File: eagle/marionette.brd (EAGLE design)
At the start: 160.3 x 174 mm, 64 parts, among them J2 SWD_CONNECTOR, J3 2X10FE, J4 2X10FE, J5 2X10FE, J6 2X10FE, J7 2X10FE, U1 USB3318, U2 NCP705, U3 XCL206B, X1 ABS25-32.768KHZ-6-T

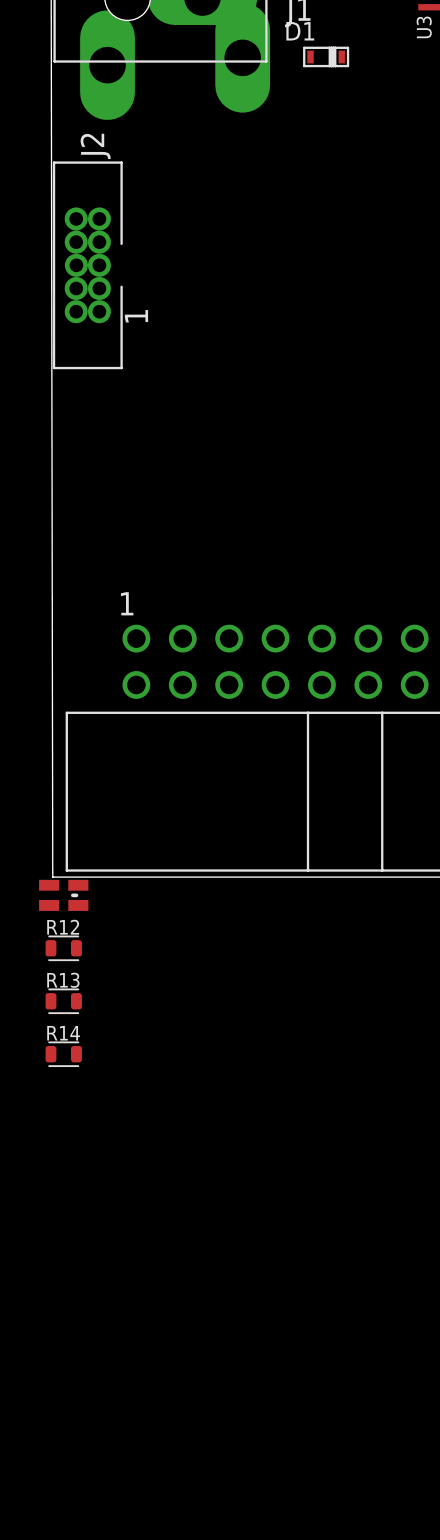
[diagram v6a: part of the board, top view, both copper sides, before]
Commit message: library update/maintinence and added pullup and pulldown resisters
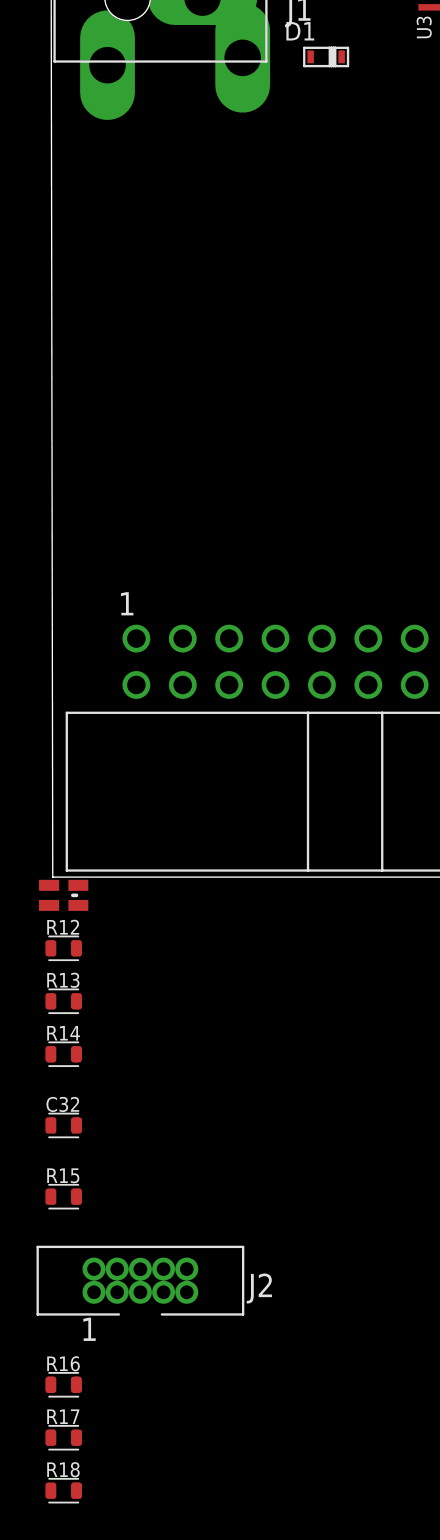
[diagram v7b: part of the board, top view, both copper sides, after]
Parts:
- added C32: 1uF, 10V, rcl_custom:.0603-C
- added R15: 820, rcl_custom:.0603-C
- added R16, R17, R18: 10k, rcl_custom:.0603-C
- J2: value SWD_CONNECTOR -> SWD
- R12: value (none) -> 68
- R13, R14: value (none) -> 5.1
- moved J2 55.7 mm to (4.80, -22.1), turned to 0 degrees
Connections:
- removed net N$13: C31.1, U$1.31, U$15.3, U$15.4
- new net NRST: C31.1, J2.10, R18.1, U$1.31, U$15.3, U$15.4
- net +3.3VDD: now also R16.2, R17.2, R18.2
- net GND: now also C28.2, C32.2, R1.2, U1.PAD
- net N$12: now also R15.2, U1.2; no longer C28.2, R1.2, U1.PAD
- net N$2: now also C32.1, R15.1; no longer U1.2
- net SWDIO: now also R17.1
- net SWO: now also R16.1

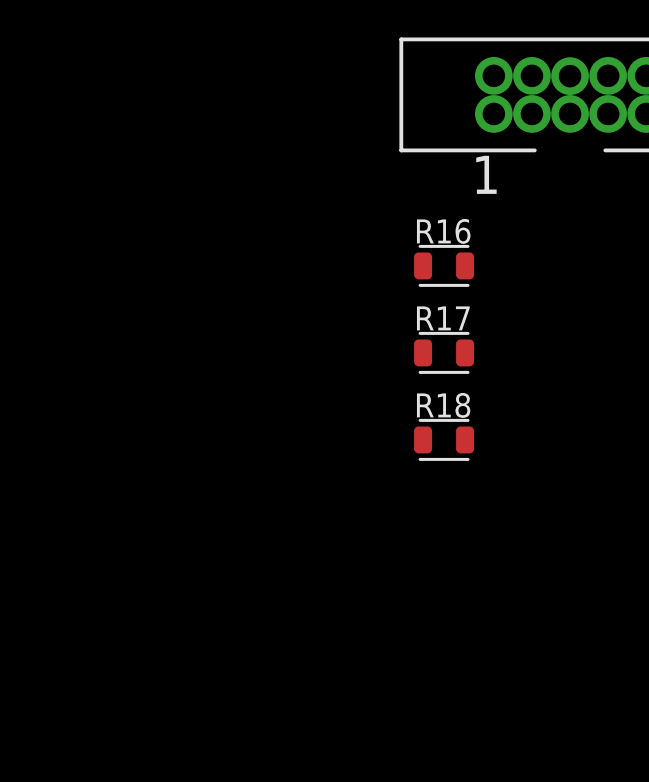
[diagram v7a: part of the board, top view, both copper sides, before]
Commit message: Added super cap and circuitry
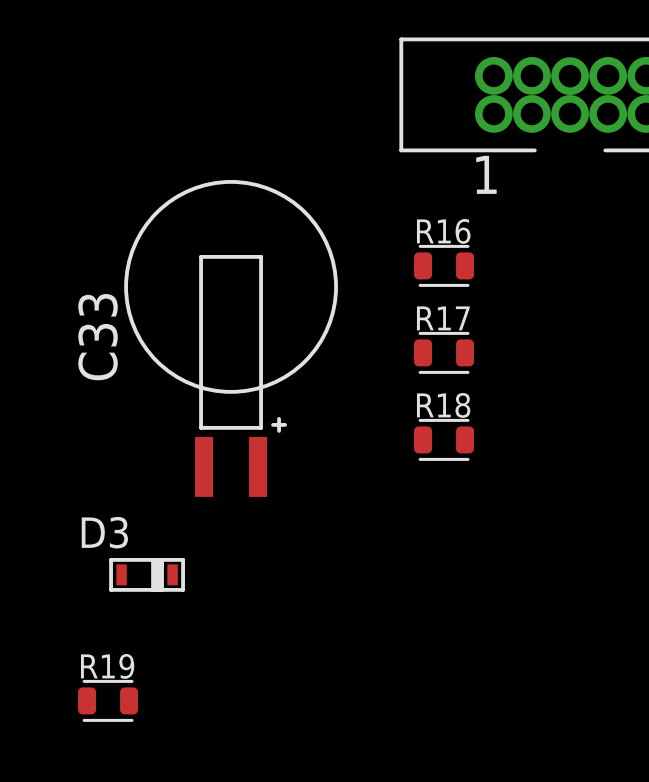
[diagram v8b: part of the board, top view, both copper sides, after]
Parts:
- added C33: EDLC, DCK3R3:SCAP
- added D3: CDBU0530, CBDU0530:SOD-523F
- added R19: (no value), rcl_custom:.0603-C
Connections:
- new net N$13: D3.P$1, R19.1
- new net N$15: C33.P, D3.P$2, U$1.6
- net +3.3VDD: now also R19.2
- net GND: now also C33.N
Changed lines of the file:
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@@
 <element name="R17" library="rcl_custom" package=".0603-C" value="10k" x="0.6" y="-30.7"/>
 <element name="R18" library="rcl_custom" package=".0603-C" value="10k" x="0.6" y="-33.6"/>
+<element name="C33" library="DCK3R3" package="SCAP" value="EDLC" x="-6.5" y="-34.5"/>
+<element name="D3" library="CBDU0530" package="SOD-523F" value="CDBU0530" x="-9.3" y="-38.1"/>
+<element name="R19" library="rcl_custom" package=".0603-C" value="" x="-10.6" y="-42.3"/>
 </elements>
 <signals>
@@
 <contactref element="J2" pad="5"/>
 <contactref element="J2" pad="3"/>
+<contactref element="C33" pad="N"/>
 <wire x1="48.422" y1="87.755" x2="48.772" y2="96.005" width="0" layer="19" extent="1-1"/>
 <wire x1="40.472" y1="87.63" x2="48.422" y2="87.755" width="0" layer="19" extent="1-1"/>
@@
 <wire x1="3.53" y1="-22.735" x2="1.3" y2="-13.6" width="0" layer="19" extent="1-1"/>
 <wire x1="4.8" y1="-22.735" x2="3.53" y2="-22.735" width="0" layer="19" extent="1-1"/>
+<wire x1="-7.4" y1="-34.5" x2="3.53" y2="-22.735" width="0" layer="19" extent="1-1"/>
 </signal>
 <signal name="SDIO_CMD">
@@
 <contactref element="R18" pad="2"/>
 <contactref element="R17" pad="2"/>
+<contactref element="R19" pad="2"/>
 <wire x1="68.97" y1="60.07" x2="68.96" y2="61.37" width="0" layer="19" extent="1-1"/>
 <wire x1="67.46" y1="63.03" x2="68.96" y2="61.37" width="0" layer="19" extent="1-1"/>
@@
 <wire x1="1.3" y1="-30.7" x2="1.3" y2="-27.8" width="0" layer="19" extent="1-1"/>
 <wire x1="1.3" y1="-33.6" x2="1.3" y2="-30.7" width="0" layer="19" extent="1-1"/>
+<wire x1="-9.9" y1="-42.3" x2="1.3" y2="-33.6" width="0" layer="19" extent="1-1"/>
 </signal>
 <signal name="ADC1/2/3_IN2">
@@
 <wire x1="1.3" y1="-17.5" x2="27.53" y2="85.85" width="0" layer="19" extent="1-1"/>
 </signal>
+<signal name="N$15">
+<contactref element="C33" pad="P"/>
+<contactref element="U$1" pad="6"/>
+<contactref element="D3" pad="P$2"/>
+<wire x1="-5.6" y1="-34.5" x2="42.55" y2="39.32" width="0" layer="19" extent="1-1"/>
+<wire x1="-8.45" y1="-38.1" x2="-5.6" y2="-34.5" width="0" layer="19" extent="1-1"/>
+</signal>
+<signal name="N$13">
+<contactref element="D3" pad="P$1"/>
+<contactref element="R19" pad="1"/>
+<wire x1="-10.15" y1="-38.1" x2="-11.3" y2="-42.3" width="0" layer="19" extent="1-1"/>
+</signal>
 </signals>
